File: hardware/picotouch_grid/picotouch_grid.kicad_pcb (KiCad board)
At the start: 2 copper layers, 180 x 110 mm, 164 parts, among them J1 TRRS, J2 TRRS, J3 TRRS, U1 Pico, U2 TS20, U3 TS20, U5 H11L1

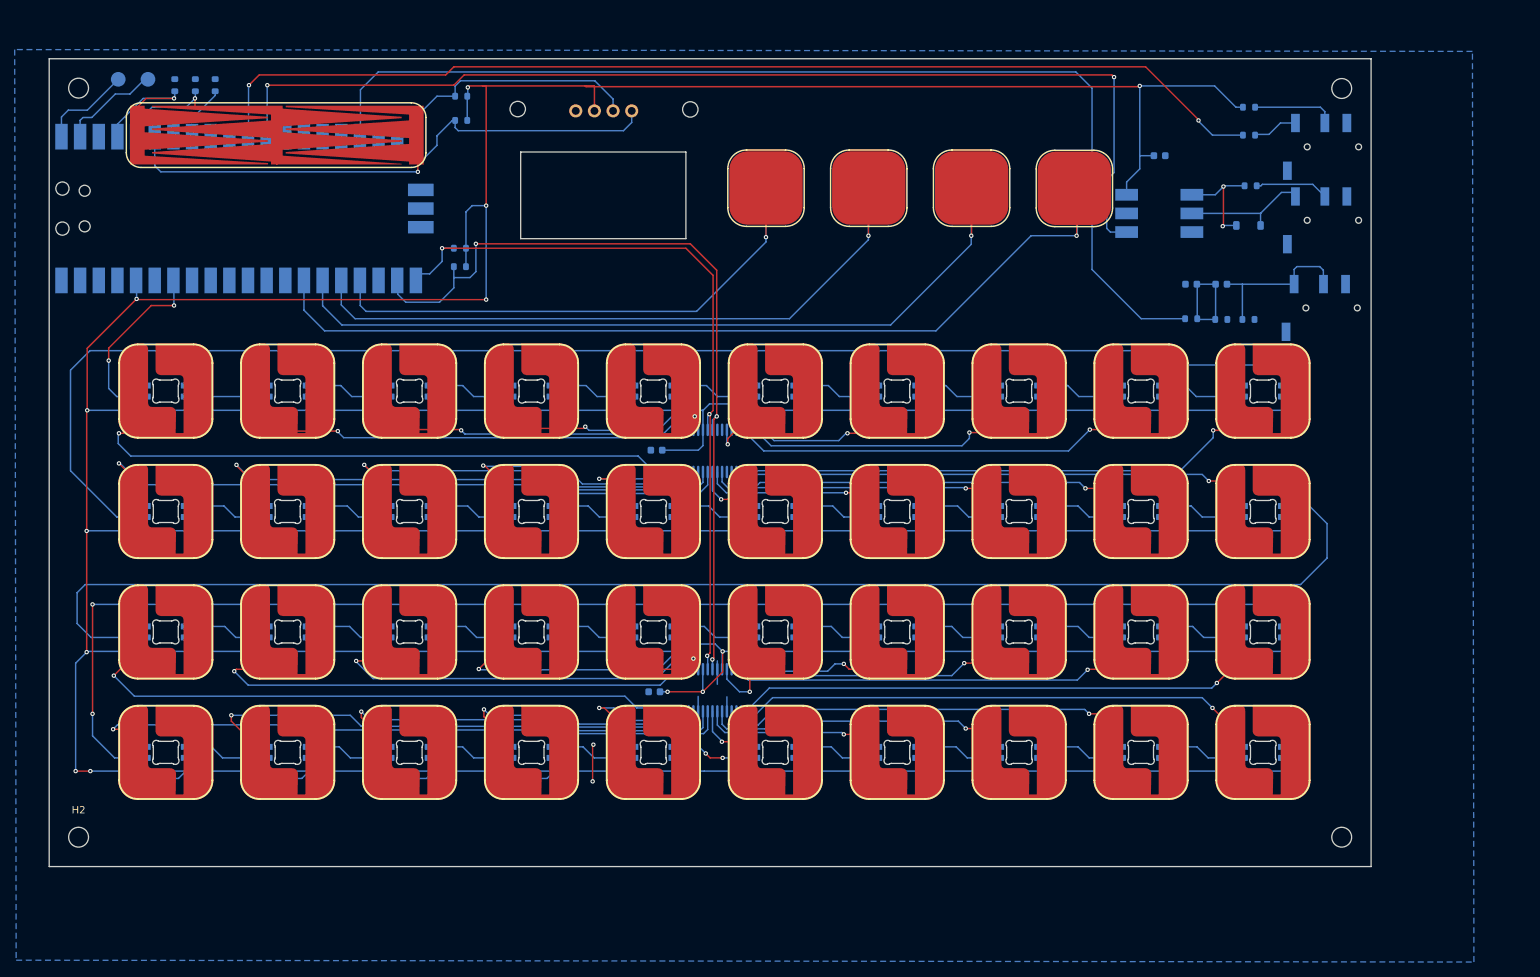
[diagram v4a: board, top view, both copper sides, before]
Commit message: pcb: another fader, i2c trace reorg
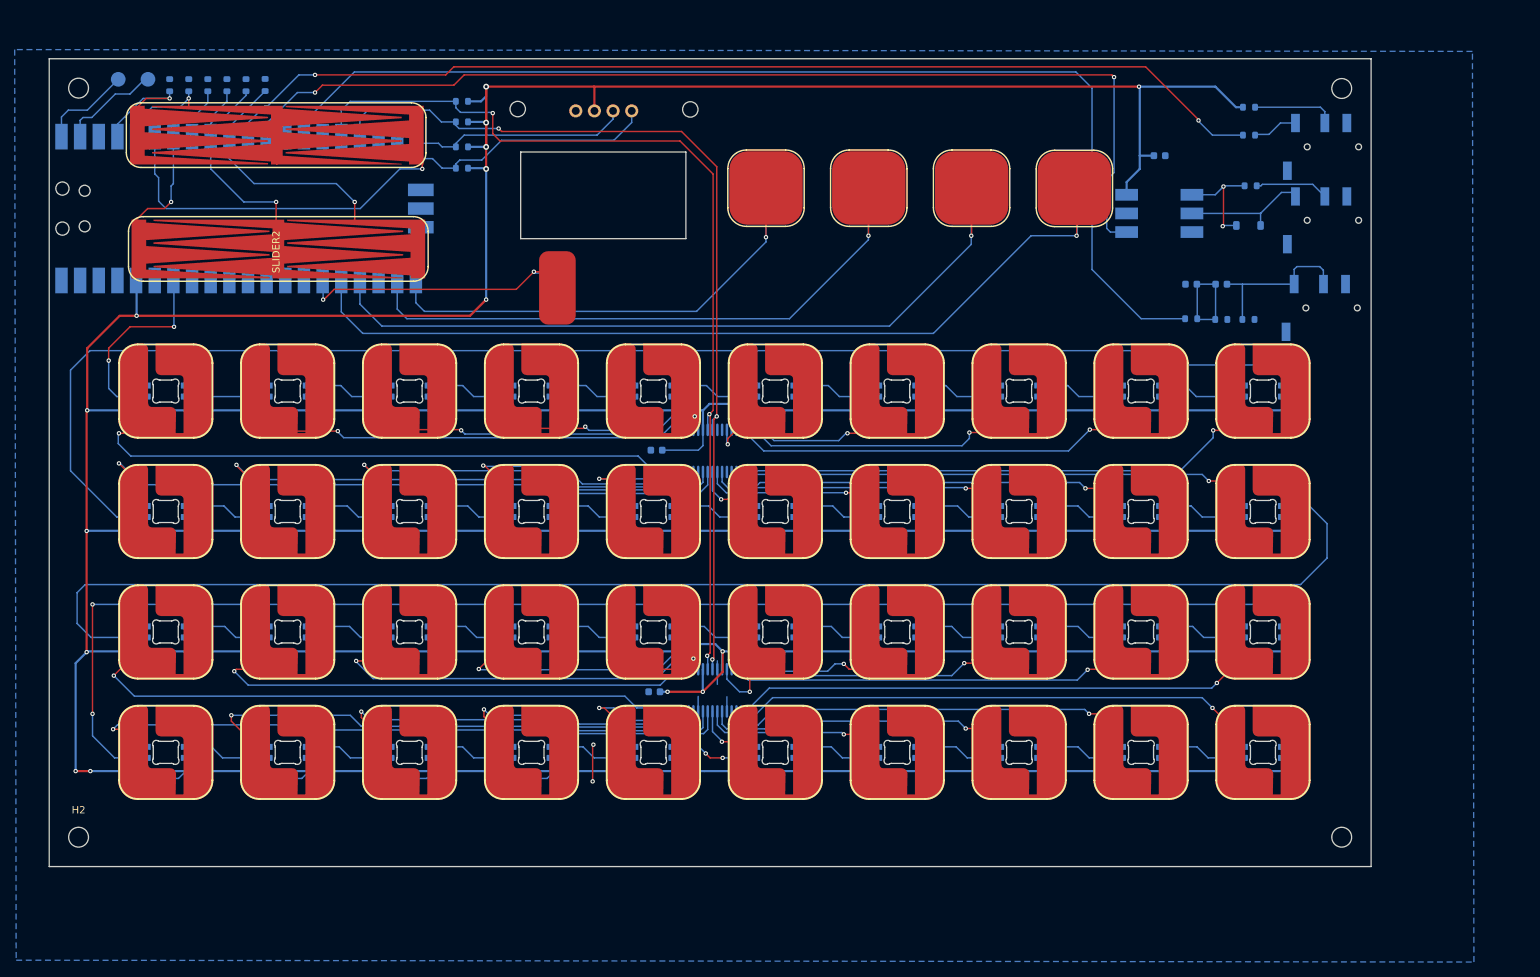
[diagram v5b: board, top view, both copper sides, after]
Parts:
- added R18: 1M, Resistor_SMD:R_0603_1608Metric, B.Cu at (99.0, 60.0)
- added R19: 1M, Resistor_SMD:R_0603_1608Metric, B.Cu at (54.2, 33.6)
- added R20: 1M, Resistor_SMD:R_0603_1608Metric, B.Cu at (56.8, 33.6)
- added R21: 1M, Resistor_SMD:R_0603_1608Metric, B.Cu at (59.4, 33.6)
- added SLIDER2: ~, todbot_eagle2023:TOUCHSLIDER3_8x40B, F.Cu at (61.2, 55.9)
- added TP45: Capacitive Button, todbot_stuff:Pad-CapacitiveTouch-SparkFun-10x5mm-roundrect, F.Cu at (99.2, 61.2)
- moved R4 20.0 mm to (86.2, 35.8)
- moved R3 19.7 mm to (86.2, 38.6)
- moved R2 6.90 mm to (86.2, 42.0)
- moved R1 6.50 mm to (86.2, 44.9)
- moved R13 1.00 mm to (51.6, 33.6)
- moved R12 0.90 mm to (49.0, 33.6)
- moved R11 0.70 mm to (46.4, 33.6)
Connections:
- U1 pad 10: unconnected-(U1-GPIO7-Pad10) -> /FADER2C
- U1 pad 14: unconnected-(U1-GPIO10-Pad14) -> /PWM_AUDIO
- U1 pad 16: unconnected-(U1-GPIO12-Pad16) -> /TOUCH_SDA
- U1 pad 17: /PWM_AUDIO -> /TOUCH_SCL
- U1 pad 21: /TOUCH_SDA -> /BUT1
- U1 pad 22: /TOUCH_SCL -> /BUT2
- U1 pad 24: /BUT1 -> /BUT3
- U1 pad 25: /BUT2 -> /BUT4
- U1 pad 26: /BUT3 -> /BUT5
- U1 pad 27: /BUT4 -> /BUT6
- U1 pad 7: unconnected-(U1-GPIO5-Pad7) -> /FADER2A
- U1 pad 9: unconnected-(U1-GPIO6-Pad9) -> /FADER2B
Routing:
- net /BUT5: track 0.00 -> 41.0 mm, vias 0 -> 2
- net /FADER2A: track 0.00 -> 37.3 mm, vias 0 -> 1
- net /FADER2C: track 0.00 -> 36.3 mm, vias 0 -> 1
- net /FADER2B: track 0.00 -> 34.2 mm, vias 0 -> 1
- net /TOUCH_SDA: track 102.4 -> 132.0 mm
- net /TOUCH_SCL: track 112.7 -> 126.8 mm
- net /BUT2: track 90.5 -> 83.3 mm
- net /BUT1: track 76.7 -> 70.1 mm
- net /FADER1C: track 54.8 -> 61.1 mm
- net /DISP_SCL: track 36.0 -> 29.9 mm
- net /BUT3: track 108.4 -> 103.3 mm
- net /PWM_AUDIO: track 149.0 -> 154.1 mm
- net /BUT4: track 125.4 -> 120.8 mm
- net /MIDI_IN: track 147.9 -> 144.9 mm
- net +3V3: track 1096.6 -> 1098.7 mm, vias 13 -> 15
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
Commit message: pcb: button layout tune
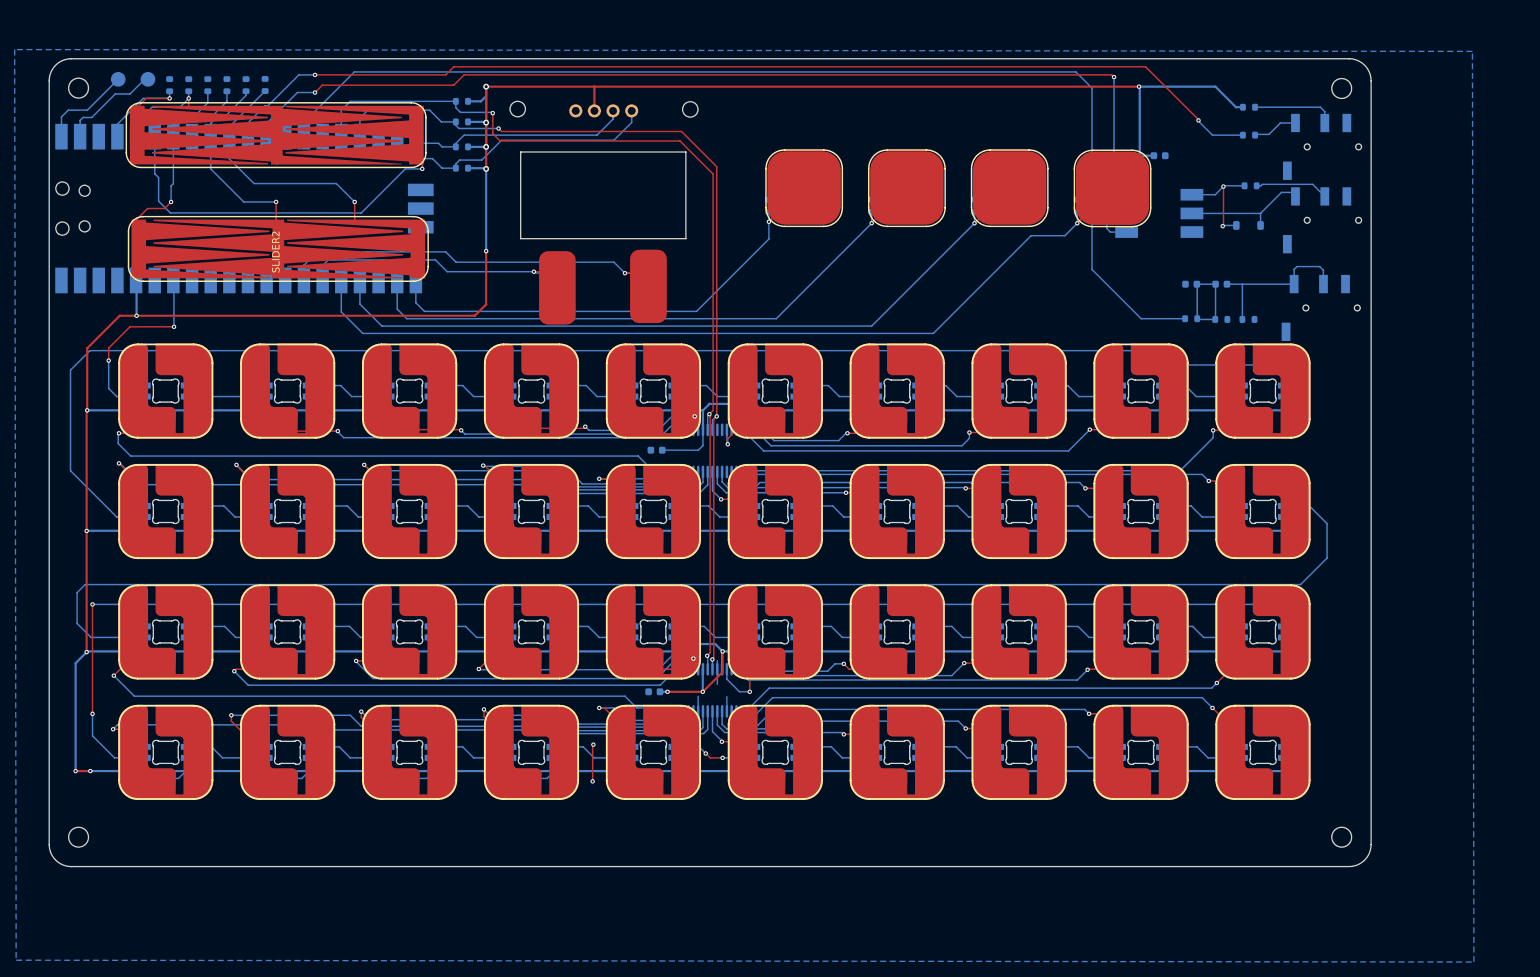
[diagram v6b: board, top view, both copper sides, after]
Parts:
- added R22: 1M, Resistor_SMD:R_0603_1608Metric, B.Cu at (111.6, 60.0)
- added TP46: Capacitive Button, todbot_stuff:Pad-CapacitiveTouch-SparkFun-10x5mm-roundrect, F.Cu at (111.6, 61.0)
- moved TP41 5.19 mm to (132.8, 47.6)
- moved TP42 5.19 mm to (146.8, 47.6)
- moved TP43 5.19 mm to (160.8, 47.6)
- moved TP44 5.19 mm to (174.8, 47.6)
- moved R15 1.21 mm to (142.0, 50.0)
- moved R14 1.17 mm to (128.0, 50.0)
- moved R17 1.10 mm to (170.0, 50.0)
- moved R16 1.03 mm to (156.0, 50.0)
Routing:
- net /BUT6: track 0.00 -> 54.0 mm, vias 0 -> 1
- net /BUT1: track 70.1 -> 67.0 mm
- net /BUT5: track 41.0 -> 38.2 mm, vias 2 -> 1
- net /BUT4: track 120.8 -> 123.5 mm
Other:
- outline, holes or cut-outs redrawn

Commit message: getting back into this, updated some stuff, getting lots of ERC, got some power pins wrong?
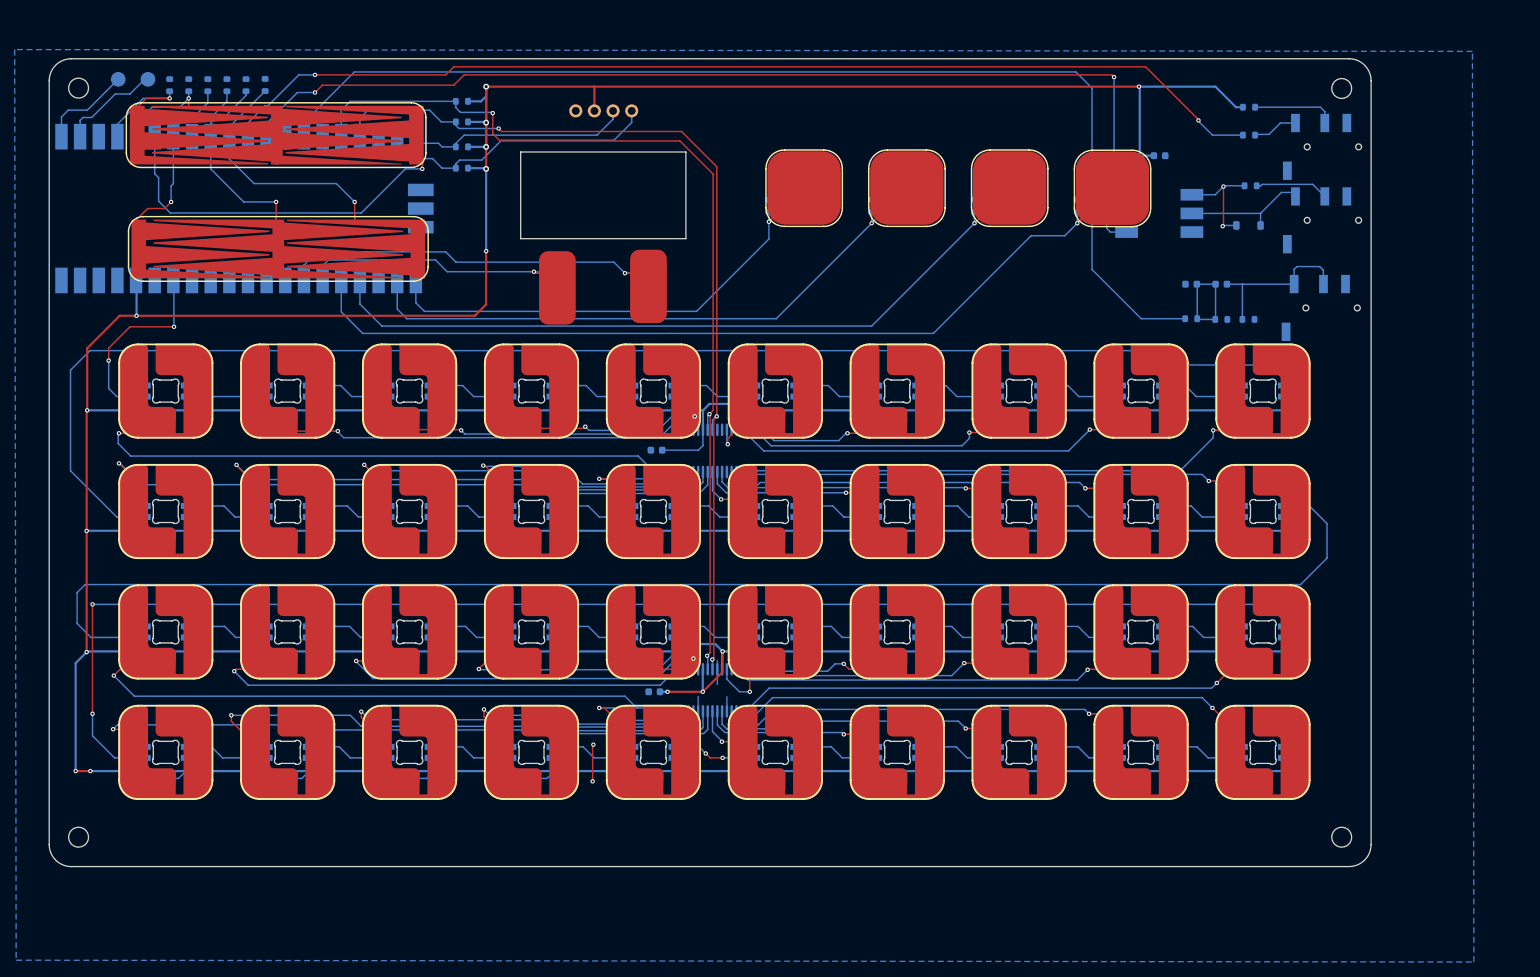
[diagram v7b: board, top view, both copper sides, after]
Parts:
- removed H5, H6: MountingHole, MountingHole:MountingHole_2.1mm
